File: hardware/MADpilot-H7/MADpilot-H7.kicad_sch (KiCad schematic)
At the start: 0 parts

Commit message: feat(hardware): capture MCU and Power schematics (#12)
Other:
- added sheet MCU (MCU.kicad_sch)
- added sheet POWER (POWER.kicad_sch)
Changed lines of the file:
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@@
     (comment 4 "License: CERN-OHL-S-2.0")
+  )
+  (sheet (at 50.8 50.8) (size 76.2 63.5)
+    (fields_autoplaced yes)
+    (stroke (width 0.1524) (type solid))
+    (fill (color 0 0 0 0.0000))
+    (property "Sheetname" "POWER" (at 50.8 49.53 0)
+      (effects (font (size 1.27 1.27)) (justify left bottom))
+    )
+    (property "Sheetfile" "POWER.kicad_sch" (at 50.8 115.57 0)
+      (effects (font (size 1.27 1.27)) (justify left top))
+    )
+    (pin "VBAT" input (at 50.8 63.5 180)
+      (effects (font (size 1.27 1.27)) (justify right))
+    )
+    (pin "VBUS" input (at 50.8 76.2 180)
+      (effects (font (size 1.27 1.27)) (justify right))
+    )
+    (pin "+5V" output (at 127.0 63.5 0)
+      (effects (font (size 1.27 1.27)) (justify left))
+    )
+    (pin "3V3_MCU" output (at 127.0 76.2 0)
+      (effects (font (size 1.27 1.27)) (justify left))
+    )
+    (pin "3V3_SENS" output (at 127.0 88.9 0)
+      (effects (font (size 1.27 1.27)) (justify left))
+    )
+    (pin "GND" power_in (at 50.8 88.9 180)
+      (effects (font (size 1.27 1.27)) (justify right))
+    )
+  )
+  (sheet (at 152.4 50.8) (size 76.2 63.5)
+    (fields_autoplaced yes)
+    (stroke (width 0.1524) (type solid))
+    (fill (color 0 0 0 0.0000))
+    (property "Sheetname" "MCU" (at 152.4 49.53 0)
+      (effects (font (size 1.27 1.27)) (justify left bottom))
+    )
+    (property "Sheetfile" "MCU.kicad_sch" (at 152.4 115.57 0)
+      (effects (font (size 1.27 1.27)) (justify left top))
+    )
+    (pin "3V3_MCU" input (at 152.4 63.5 180)
+      (effects (font (size 1.27 1.27)) (justify right))
+    )
+    (pin "3V3_SENS" input (at 152.4 76.2 180)
+      (effects (font (size 1.27 1.27)) (justify right))
+    )
+    (pin "+5V" input (at 152.4 88.9 180)
+      (effects (font (size 1.27 1.27)) (justify right))
+    )
+    (pin "GND" power_in (at 152.4 101.6 180)
+      (effects (font (size 1.27 1.27)) (justify right))
+    )
   )
   (sheet_instances
@@
       (page "1")
     )
+    (path "/c50d4f61-231a-4d2b-986a-723a10526e01"
+      (page "2")
+    )
+    (path "/020f93d0-ab76-4c08-9373-958d923a454f"
+      (page "3")
+    )
   )

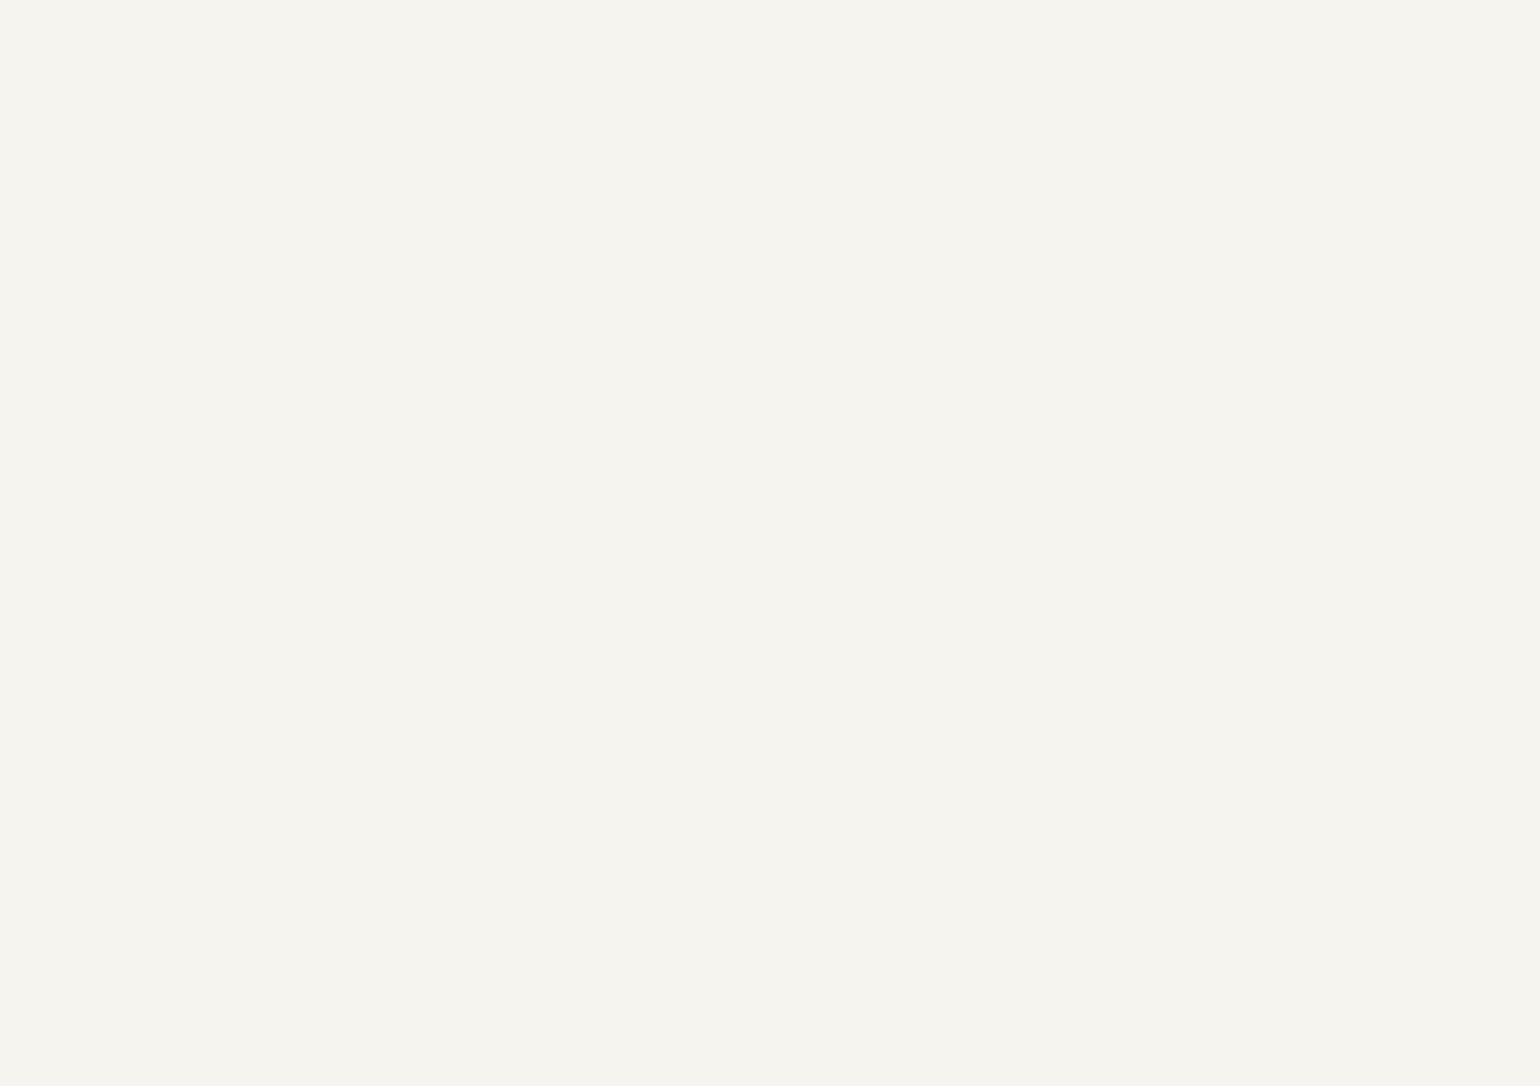
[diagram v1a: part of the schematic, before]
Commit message: feat(hardware): capture sensor suite and dual CAN bus schematics (#13)
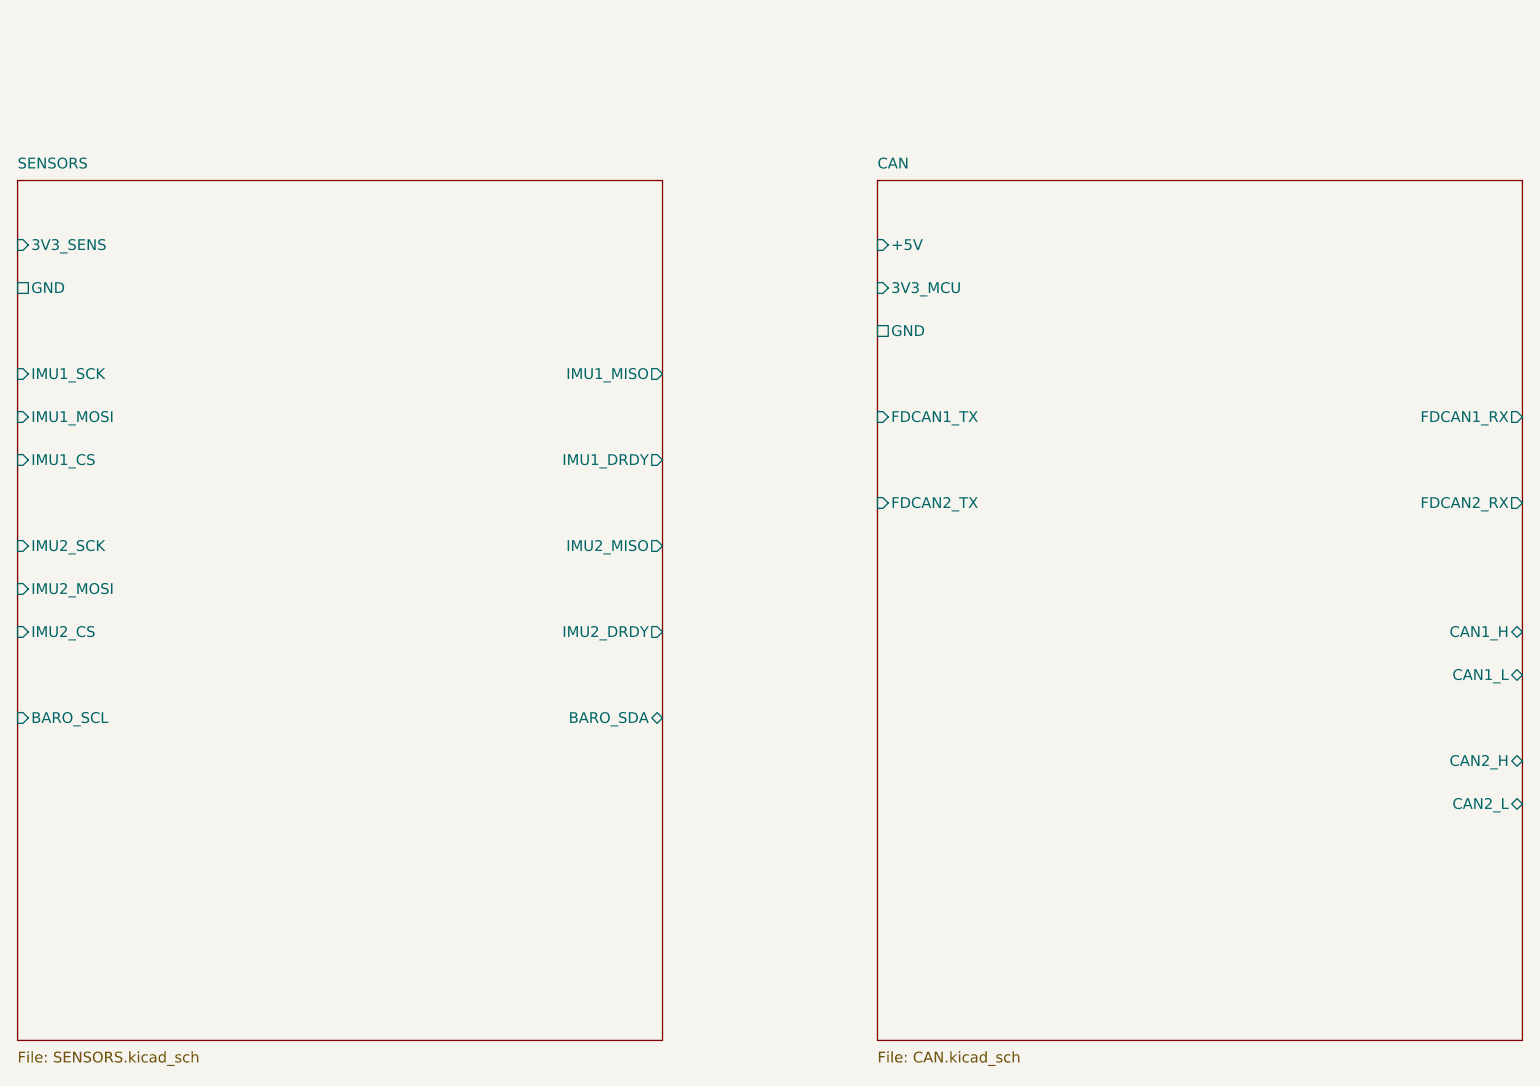
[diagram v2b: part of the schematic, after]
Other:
- added sheet CAN (CAN.kicad_sch)
- added sheet SENSORS (SENSORS.kicad_sch)
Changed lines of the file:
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@@
+    )
+  )
+  (sheet (at 50.8 139.7) (size 76.2 101.6)
+    (fields_autoplaced yes)
+    (stroke (width 0.1524) (type solid))
+    (fill (color 0 0 0 0.0000))
+    (property "Sheetname" "SENSORS" (at 50.8 138.43 0)
+      (effects (font (size 1.27 1.27)) (justify left bottom))
+    )
+    (property "Sheetfile" "SENSORS.kicad_sch" (at 50.8 242.57 0)
+      (effects (font (size 1.27 1.27)) (justify left top))
+    )
+    (pin "3V3_SENS" input (at 50.8 147.32 180)
+      (effects (font (size 1.27 1.27)) (justify right))
+    )
+    (pin "GND" power_in (at 50.8 152.4 180)
+      (effects (font (size 1.27 1.27)) (justify right))
+    )
+    (pin "IMU1_SCK" input (at 50.8 162.56 180)
+      (effects (font (size 1.27 1.27)) (justify right))
+    )
+    (pin "IMU1_MISO" output (at 127.0 162.56 0)
+      (effects (font (size 1.27 1.27)) (justify left))
+    )
+    (pin "IMU1_MOSI" input (at 50.8 167.64 180)
+      (effects (font (size 1.27 1.27)) (justify right))
+    )
+    (pin "IMU1_CS" input (at 50.8 172.72 180)
+      (effects (font (size 1.27 1.27)) (justify right))
+    )
+    (pin "IMU1_DRDY" output (at 127.0 172.72 0)
+      (effects (font (size 1.27 1.27)) (justify left))
+    )
+    (pin "IMU2_SCK" input (at 50.8 182.88 180)
+      (effects (font (size 1.27 1.27)) (justify right))
+    )
+    (pin "IMU2_MISO" output (at 127.0 182.88 0)
+      (effects (font (size 1.27 1.27)) (justify left))
+    )
+    (pin "IMU2_MOSI" input (at 50.8 187.96 180)
+      (effects (font (size 1.27 1.27)) (justify right))
+    )
+    (pin "IMU2_CS" input (at 50.8 193.04 180)
+      (effects (font (size 1.27 1.27)) (justify right))
+    )
+    (pin "IMU2_DRDY" output (at 127.0 193.04 0)
+      (effects (font (size 1.27 1.27)) (justify left))
+    )
+    (pin "BARO_SCL" input (at 50.8 203.2 180)
+      (effects (font (size 1.27 1.27)) (justify right))
+    )
+    (pin "BARO_SDA" bidirectional (at 127.0 203.2 0)
+      (effects (font (size 1.27 1.27)) (justify left))
+    )
+  )
+  (sheet (at 152.4 139.7) (size 76.2 101.6)
+    (fields_autoplaced yes)
+    (stroke (width 0.1524) (type solid))
+    (fill (color 0 0 0 0.0000))
+    (property "Sheetname" "CAN" (at 152.4 138.43 0)
+      (effects (font (size 1.27 1.27)) (justify left bottom))
+    )
+    (property "Sheetfile" "CAN.kicad_sch" (at 152.4 242.57 0)
+      (effects (font (size 1.27 1.27)) (justify left top))
+    )
+    (pin "+5V" input (at 152.4 147.32 180)
+      (effects (font (size 1.27 1.27)) (justify right))
+    )
+    (pin "3V3_MCU" input (at 152.4 152.4 180)
+      (effects (font (size 1.27 1.27)) (justify right))
+    )
+    (pin "GND" power_in (at 152.4 157.48 180)
+      (effects (font (size 1.27 1.27)) (justify right))
+    )
+    (pin "FDCAN1_TX" input (at 152.4 167.64 180)
+      (effects (font (size 1.27 1.27)) (justify right))
+    )
+    (pin "FDCAN1_RX" output (at 228.6 167.64 0)
+      (effects (font (size 1.27 1.27)) (justify left))
+    )
+    (pin "FDCAN2_TX" input (at 152.4 177.8 180)
+      (effects (font (size 1.27 1.27)) (justify right))
+    )
+    (pin "FDCAN2_RX" output (at 228.6 177.8 0)
+      (effects (font (size 1.27 1.27)) (justify left))
+    )
+    (pin "CAN1_H" bidirectional (at 228.6 193.04 0)
+      (effects (font (size 1.27 1.27)) (justify left))
+    )
+    (pin "CAN1_L" bidirectional (at 228.6 198.12 0)
+      (effects (font (size 1.27 1.27)) (justify left))
+    )
+    (pin "CAN2_H" bidirectional (at 228.6 208.28 0)
+      (effects (font (size 1.27 1.27)) (justify left))
+    )
+    (pin "CAN2_L" bidirectional (at 228.6 213.36 0)
+      (effects (font (size 1.27 1.27)) (justify left))
     )
   )
@@
       (page "3")
     )
+    (path "/e3831b34-4b51-4f04-8cb3-7a915904ef21"
+      (page "4")
+    )
+    (path "/9a184e1b-8772-4bc4-9d58-bb1936c53e02"
+      (page "5")
+    )
   )

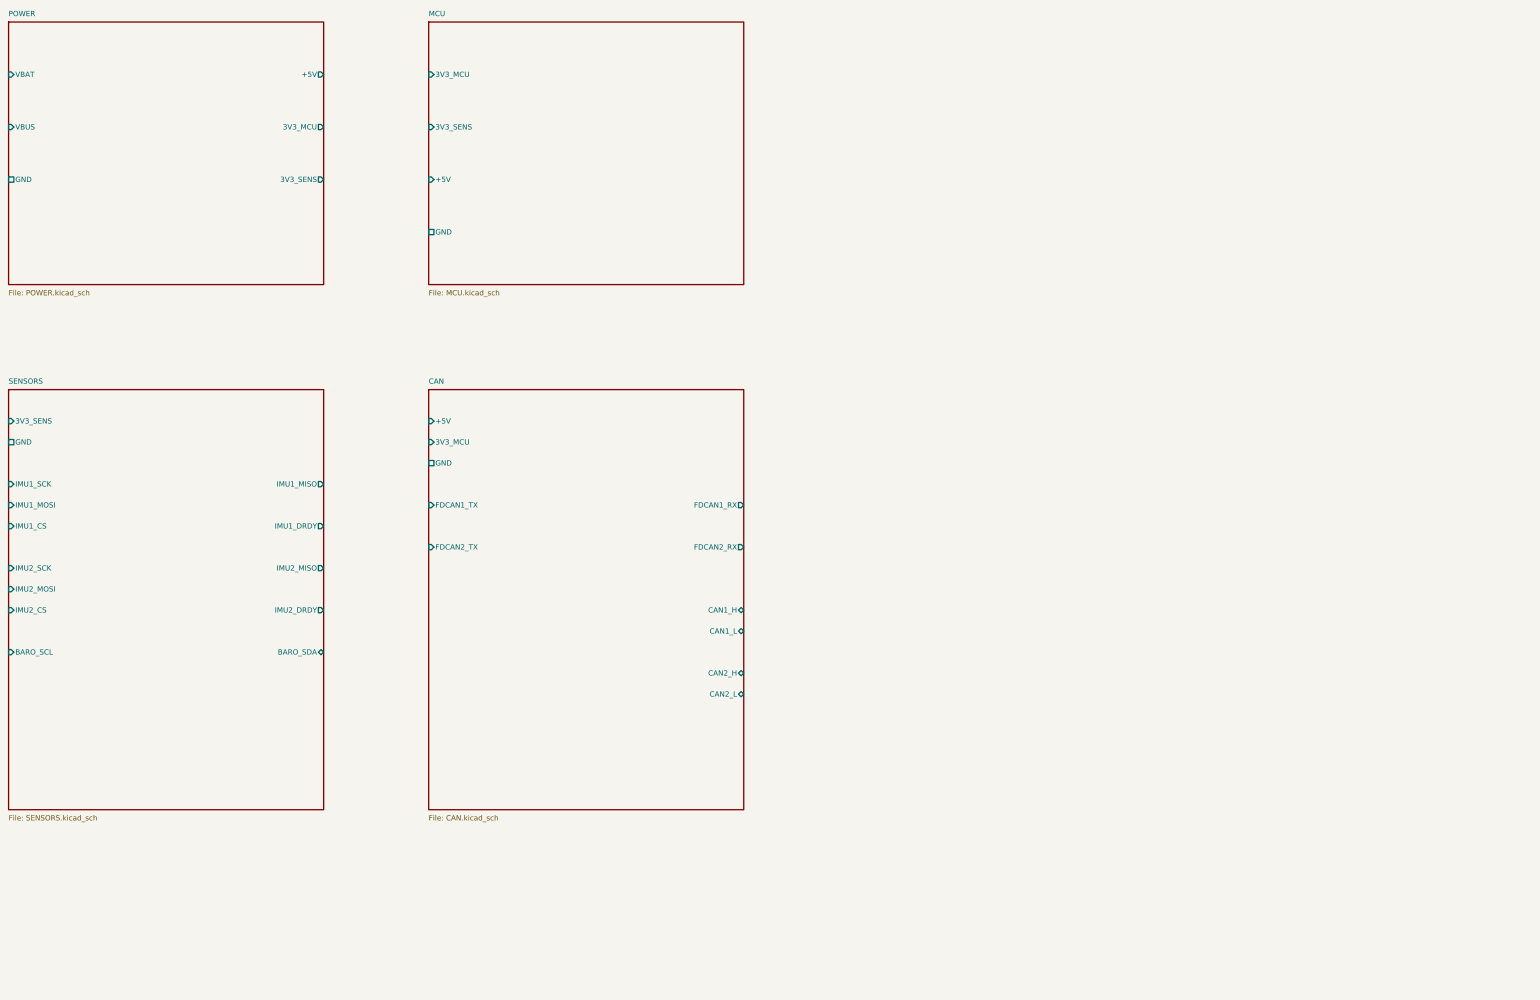
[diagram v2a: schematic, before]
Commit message: feat(hardware): capture storage, connectors, and debug schematics (#14)
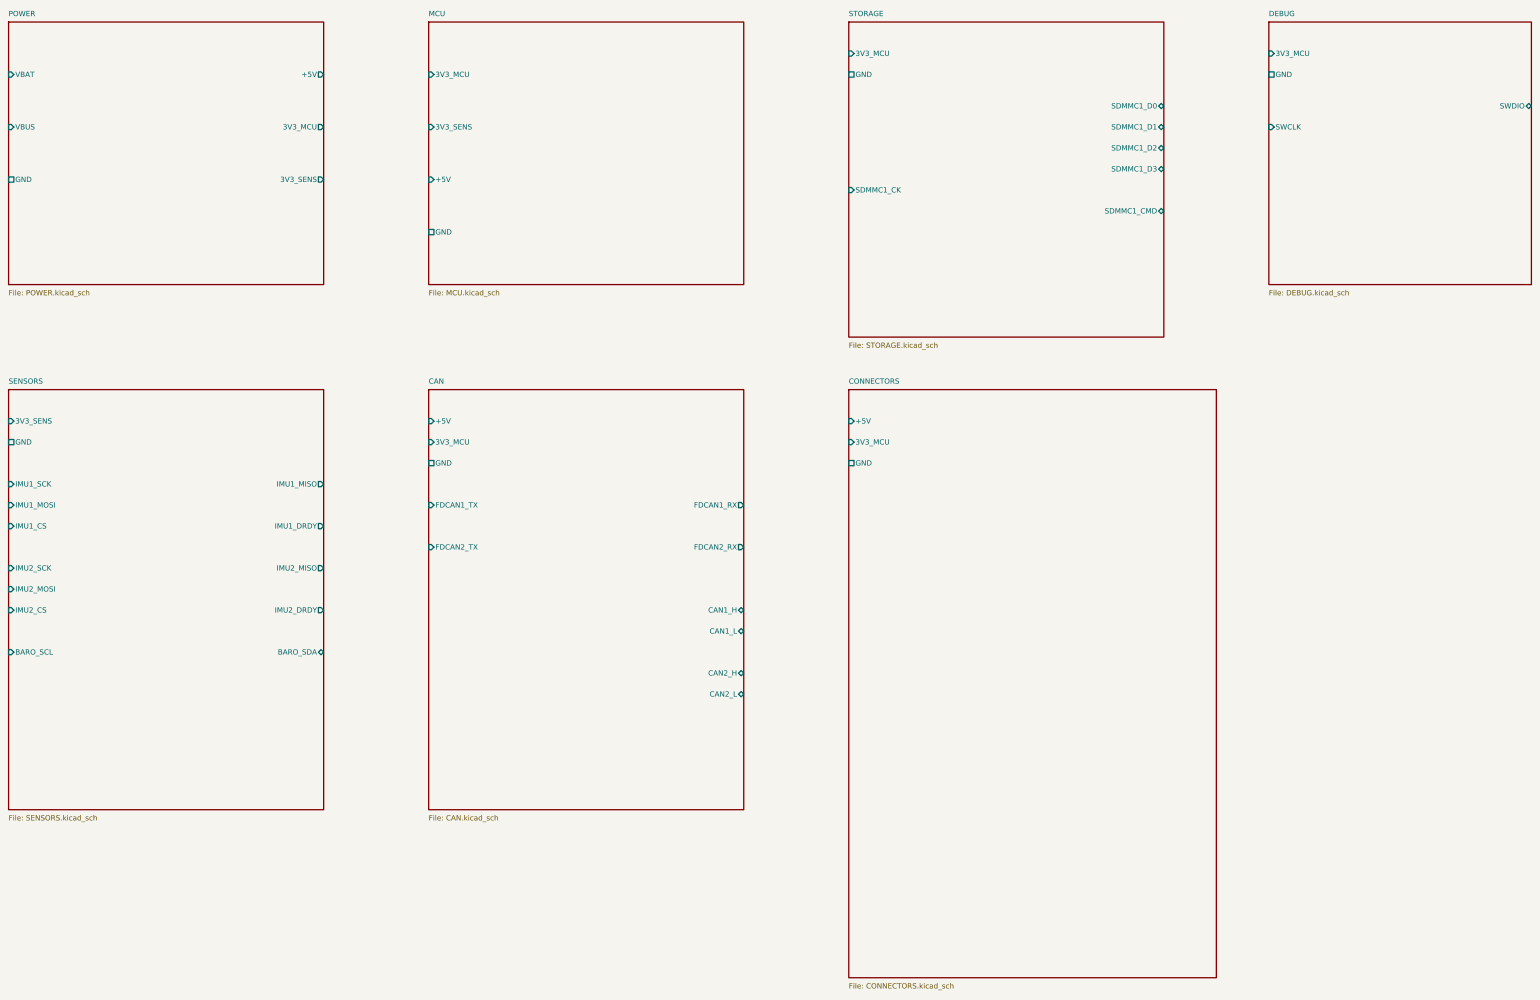
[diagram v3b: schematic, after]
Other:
- added sheet CONNECTORS (CONNECTORS.kicad_sch)
- added sheet DEBUG (DEBUG.kicad_sch)
- added sheet STORAGE (STORAGE.kicad_sch)
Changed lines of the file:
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@@
+    )
+  )
+  (sheet (at 254.0 50.8) (size 76.2 76.2)
+    (fields_autoplaced yes)
+    (stroke (width 0.1524) (type solid))
+    (fill (color 0 0 0 0.0000))
+    (property "Sheetname" "STORAGE" (at 254.0 49.53 0)
+      (effects (font (size 1.27 1.27)) (justify left bottom))
+    )
+    (property "Sheetfile" "STORAGE.kicad_sch" (at 254.0 128.27 0)
+      (effects (font (size 1.27 1.27)) (justify left top))
+    )
+    (pin "3V3_MCU" input (at 254.0 58.42 180)
+      (effects (font (size 1.27 1.27)) (justify right))
+    )
+    (pin "GND" power_in (at 254.0 63.5 180)
+      (effects (font (size 1.27 1.27)) (justify right))
+    )
+    (pin "SDMMC1_D0" bidirectional (at 330.2 71.12 0)
+      (effects (font (size 1.27 1.27)) (justify left))
+    )
+    (pin "SDMMC1_D1" bidirectional (at 330.2 76.2 0)
+      (effects (font (size 1.27 1.27)) (justify left))
+    )
+    (pin "SDMMC1_D2" bidirectional (at 330.2 81.28 0)
+      (effects (font (size 1.27 1.27)) (justify left))
+    )
+    (pin "SDMMC1_D3" bidirectional (at 330.2 86.36 0)
+      (effects (font (size 1.27 1.27)) (justify left))
+    )
+    (pin "SDMMC1_CK" input (at 254.0 91.44 180)
+      (effects (font (size 1.27 1.27)) (justify right))
+    )
+    (pin "SDMMC1_CMD" bidirectional (at 330.2 96.52 0)
+      (effects (font (size 1.27 1.27)) (justify left))
+    )
+  )
+  (sheet (at 254.0 139.7) (size 88.9 142.24)
+    (fields_autoplaced yes)
+    (stroke (width 0.1524) (type solid))
+    (fill (color 0 0 0 0.0000))
+    (property "Sheetname" "CONNECTORS" (at 254.0 138.43 0)
+      (effects (font (size 1.27 1.27)) (justify left bottom))
+    )
+    (property "Sheetfile" "CONNECTORS.kicad_sch" (at 254.0 283.21 0)
+      (effects (font (size 1.27 1.27)) (justify left top))
+    )
+    (pin "+5V" input (at 254.0 147.32 180)
+      (effects (font (size 1.27 1.27)) (justify right))
+    )
+    (pin "3V3_MCU" input (at 254.0 152.4 180)
+      (effects (font (size 1.27 1.27)) (justify right))
+    )
+    (pin "GND" power_in (at 254.0 157.48 180)
+      (effects (font (size 1.27 1.27)) (justify right))
+    )
+  )
+  (sheet (at 355.6 50.8) (size 63.5 63.5)
+    (fields_autoplaced yes)
+    (stroke (width 0.1524) (type solid))
+    (fill (color 0 0 0 0.0000))
+    (property "Sheetname" "DEBUG" (at 355.6 49.53 0)
+      (effects (font (size 1.27 1.27)) (justify left bottom))
+    )
+    (property "Sheetfile" "DEBUG.kicad_sch" (at 355.6 115.57 0)
+      (effects (font (size 1.27 1.27)) (justify left top))
+    )
+    (pin "3V3_MCU" input (at 355.6 58.42 180)
+      (effects (font (size 1.27 1.27)) (justify right))
+    )
+    (pin "GND" power_in (at 355.6 63.5 180)
+      (effects (font (size 1.27 1.27)) (justify right))
+    )
+    (pin "SWDIO" bidirectional (at 419.1 71.12 0)
+      (effects (font (size 1.27 1.27)) (justify left))
+    )
+    (pin "SWCLK" input (at 355.6 76.2 180)
+      (effects (font (size 1.27 1.27)) (justify right))
     )
   )
@@
       (page "5")
     )
+    (path "/837e2b10-c021-4d1a-8861-592f8a410e05"
+      (page "6")
+    )
+    (path "/6392a101-7132-4ba1-8931-445829bb8a06"
+      (page "7")
+    )
+    (path "/d734e101-5231-4ec1-9871-332918bb7a07"
+      (page "8")
+    )
   )
